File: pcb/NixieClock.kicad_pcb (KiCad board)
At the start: 2 copper layers, 250 x 100 mm, 227 parts, among them J1 USB_B, J2 BARREL_JACK, J3 Screw_Terminal_1x04, Q1 MMBT3906, Q10 MMBTA92, Q11 MMBTA42, Q12 MMBTA42, Q13 MMBTA42, Q14 MMBTA42, Q15 MMBTA42, Q16 MMBTA42, Q17 MMBTA92, Q18 MMBTA42, Q19 MMBTA42, Q2 STD5N52U, Q20 MMBTA42, Q21 MMBTA92, Q22 MMBTA42, Q23 MMBTA42, Q24 MMBTA42, Q25 MMBTA42, Q26 MMBTA92, Q27 MMBTA42, Q28 MMBTA42, Q29 MMBTA42, Q3 MMBTA42, Q30 MMBTA92, Q31 MMBTA42, Q32 MMBTA42, Q33 MMBTA42, Q34 MMBTA42, Q35 MMBTA92, Q36 MMBTA42, Q37 MMBTA42, Q38 Si2301CDS, Q39 MMBT3904, Q4 MMBTA42, Q40 MMBT3904, Q5 MMBTA42, Q6 MMBTA42, Q7 MMBTA42, Q8 MMBTA42, Q9 MMBTA42, SW1 SKQUCAA010, SW2 SW_Push, SW3 SW_Push, SW4 SW_Push, SW5 SW_Push, U1 DS3231, U10 MC34063A, U11 PCF8574, U12 PCF8574, U13 CD4028B, U14 74HC238, U15 74HC238, U16 74HC238, U2 PCF8574, U3 ESP-12F, U4 CH340G, U5 LM1117-3.3, U6 STA013, U7 CS4344, U8 PAM8403, U9 MC34063A, Y1 12MHz, Y2 12MHz

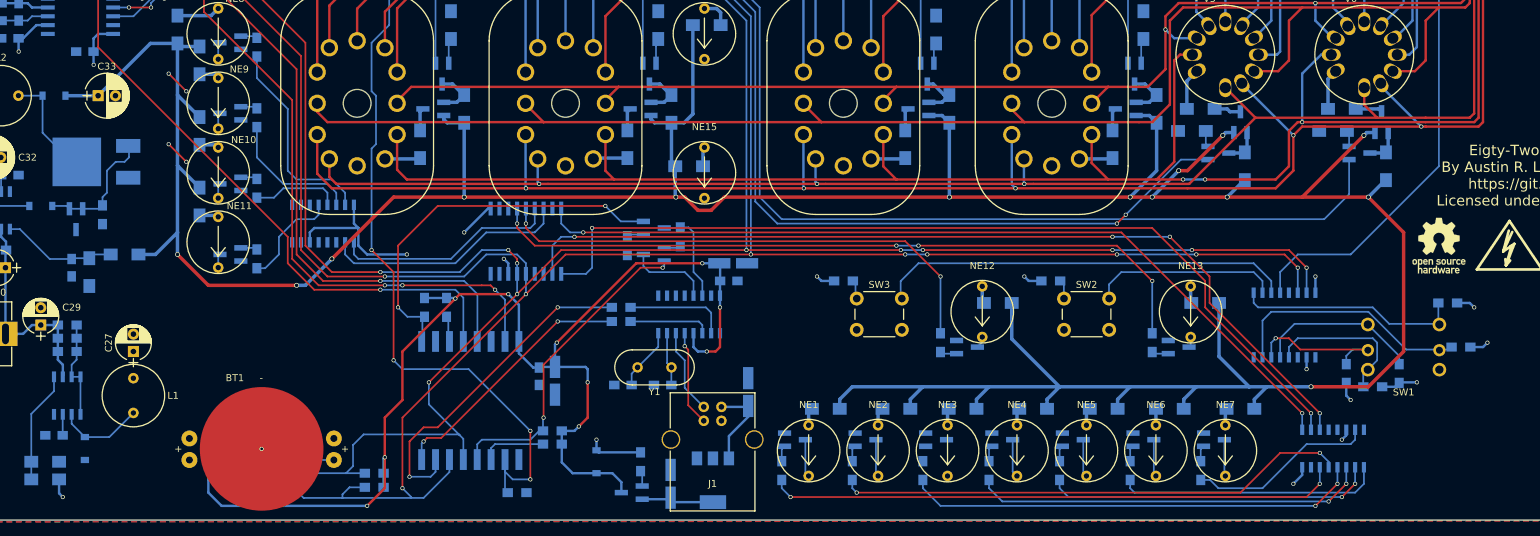
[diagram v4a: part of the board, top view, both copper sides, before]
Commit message: Swapped Q2 for cheaper STN1NK60Z. Fixed some ground plane issues.
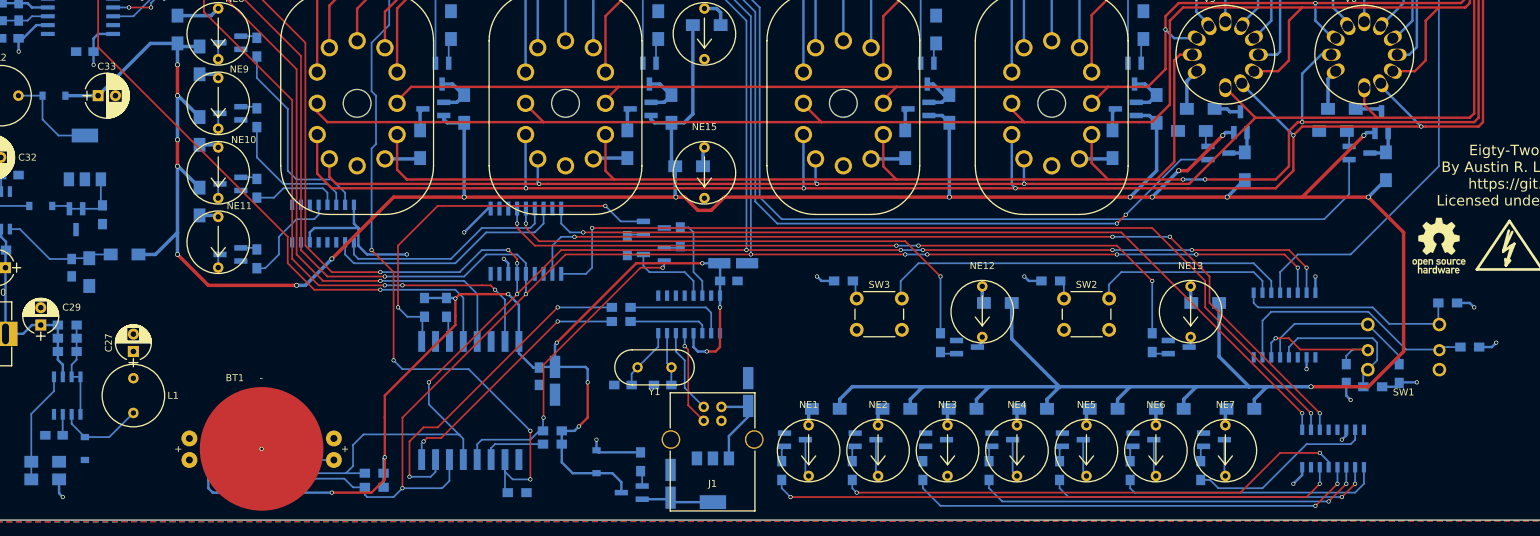
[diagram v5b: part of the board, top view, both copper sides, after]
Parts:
- Q2: value STD5N52U -> STN1NK60Z; footprint TO_SOT_Packages_SMD:TO-252-2Lead -> TO_SOT_Packages_SMD:SOT-223
- moved Q2 2.62 mm to (50.8, 97.8), turned to 90 degrees
- moved R7 1.27 mm to (250.2, 125.1)
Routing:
- net GND: track 17.1 -> 9.93 mm, vias 7 -> 3
- net Net-(D2-Pad1): track 19.2 -> 12.1 mm
- net SCL: track 350.8 -> 345.1 mm
- net USB_PWR: track 185.5 -> 182.8 mm
- net Net-(D3-Pad2): track 15.5 -> 14.0 mm
- net Net-(R7-Pad2): track 35.4 -> 36.6 mm
- net +170V: track 526.4 -> 526.8 mm, vias 14 -> 18
